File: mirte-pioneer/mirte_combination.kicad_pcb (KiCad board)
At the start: 2 copper layers, 55 x 81.9 mm, 48 parts, among them J1 Servo3, J10 IR1, J11 Conn_01x13_Female, J12 IR Object Detector 1, J14 IR2, J17 MC1, J18 MC2, J19 Servo1, J2 Conn_01x20_Female, J20 SRF1, J21 ENC2, J23 MC1-A, J24 MC1-B, J25 SRF2, J26 ENC1, J27 Servo2, J28 I2C2, J3 Servo4, J30 I2C1, J33 line out left, J34 Power in, J35 Power out, J37 on/off, J4 Conn_01x20_Female, J7 Keypad, J8 Conn_01x06_Female, J9 IR Object Detector 2, Q1 DMG2305UX, Q2 DMN2050L, SW1 on/off, U1 CH340C, U2 CH340E

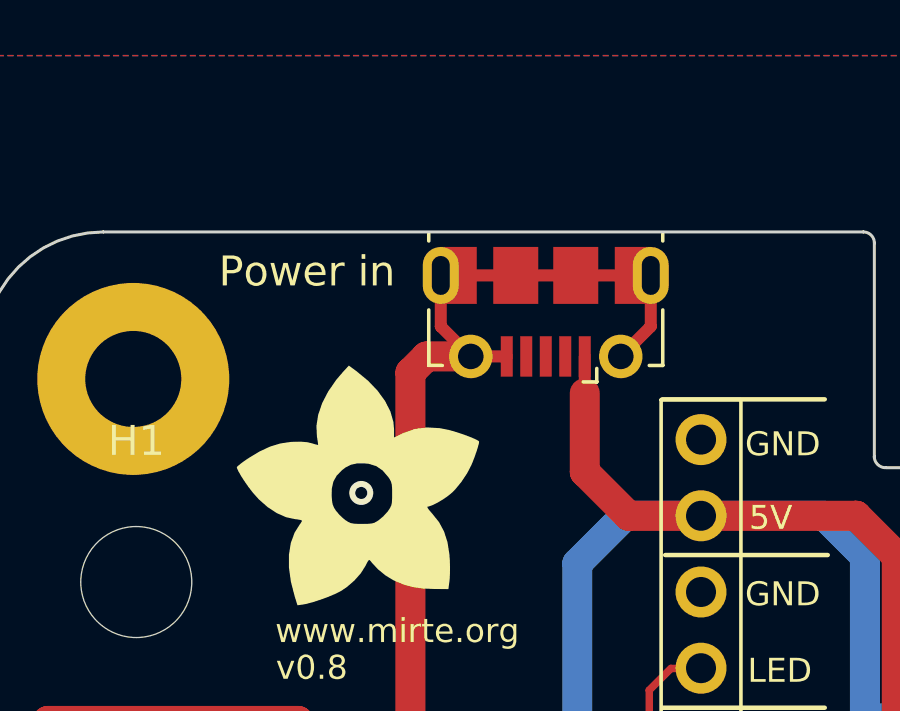
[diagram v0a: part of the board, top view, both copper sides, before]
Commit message: jlcpcb fixes mirte-pioneer
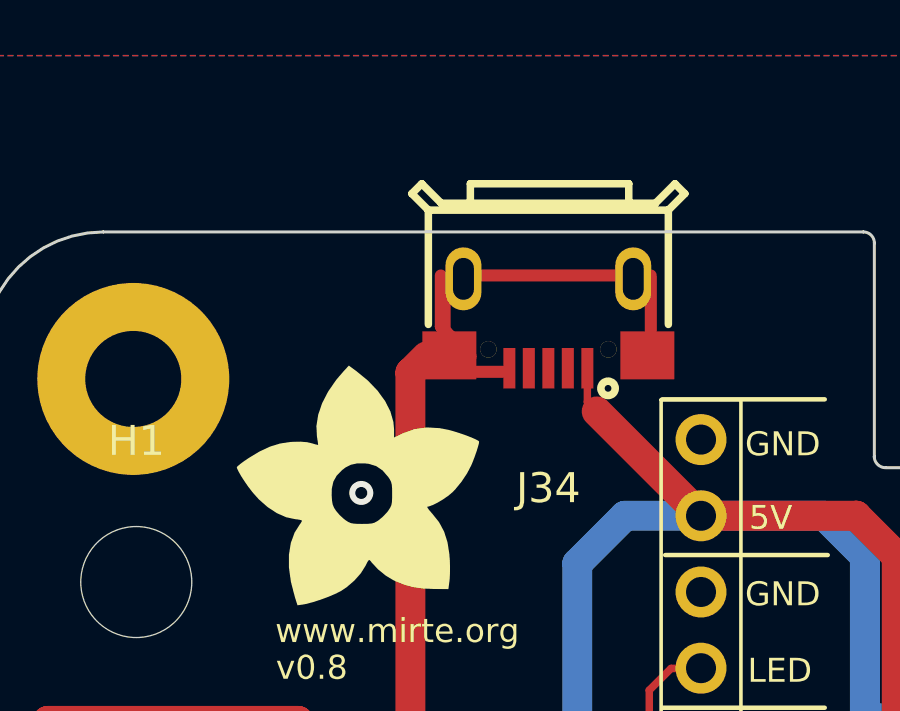
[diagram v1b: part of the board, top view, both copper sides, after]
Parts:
- J34: footprint Connector_USB:USB_Micro-B_Molex-105017-0001 -> lcsc:MICRO-USB-SMD_U254-051T-4BH83-S1S
- moved J34 0.38 mm to (118.8, 53.2)
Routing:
- net 5V: track 352.9 -> 351.1 mm
